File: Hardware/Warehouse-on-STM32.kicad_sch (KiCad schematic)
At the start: 22 parts, among them J1 ESP8266, J2 Conn_01x05, SW1 SW_Push, SW2 SW_Push, SW3 SW_Push, SW4 SW_Push, U1 STM32F103C8Tx, Y1 8MHz

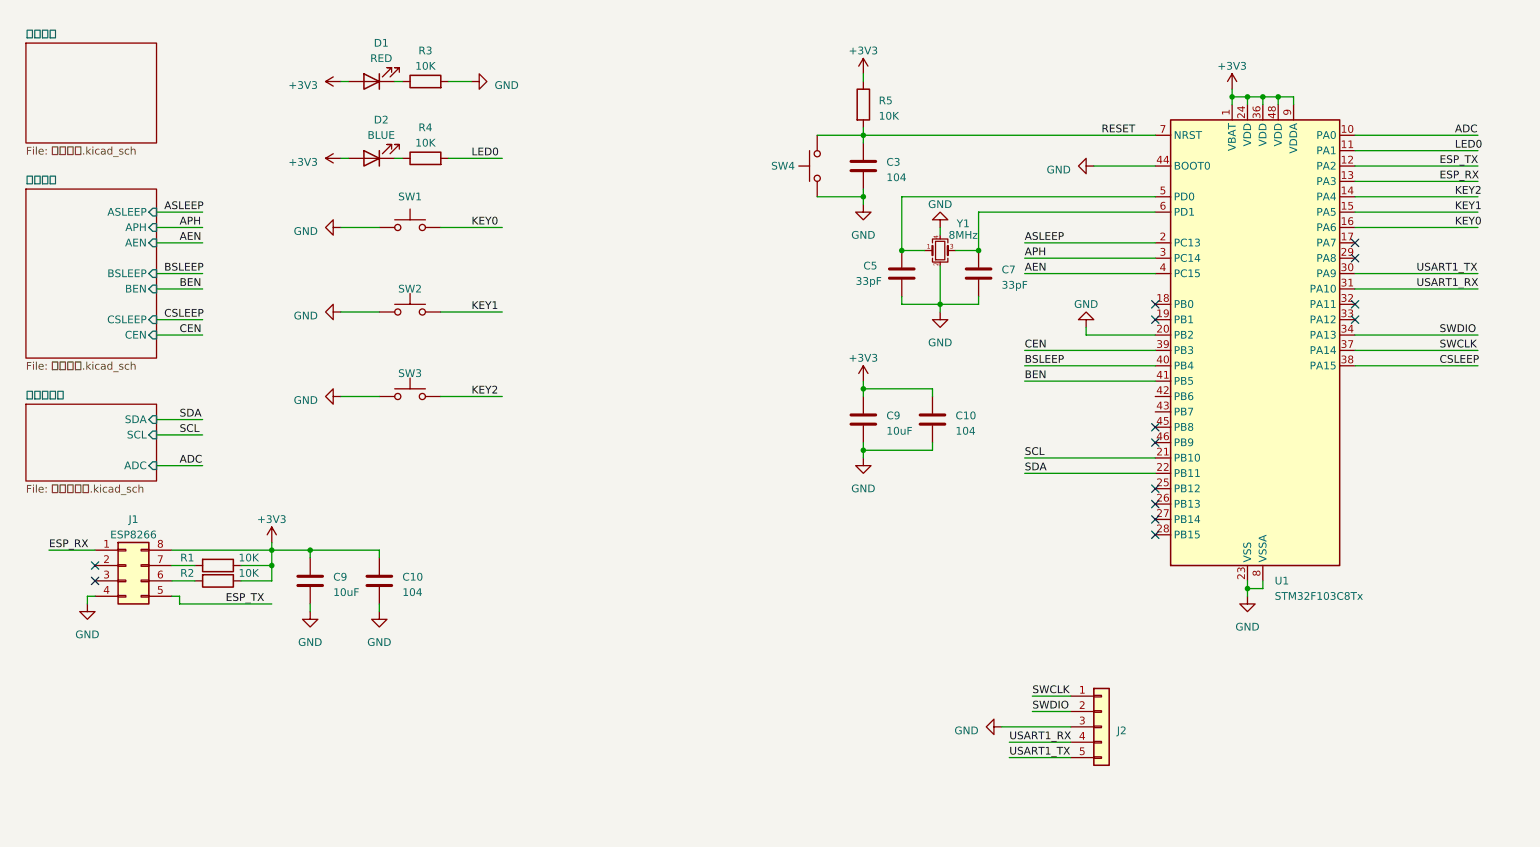
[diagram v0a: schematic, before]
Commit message: 修改了电机驱动芯片旁的电容封装为0603
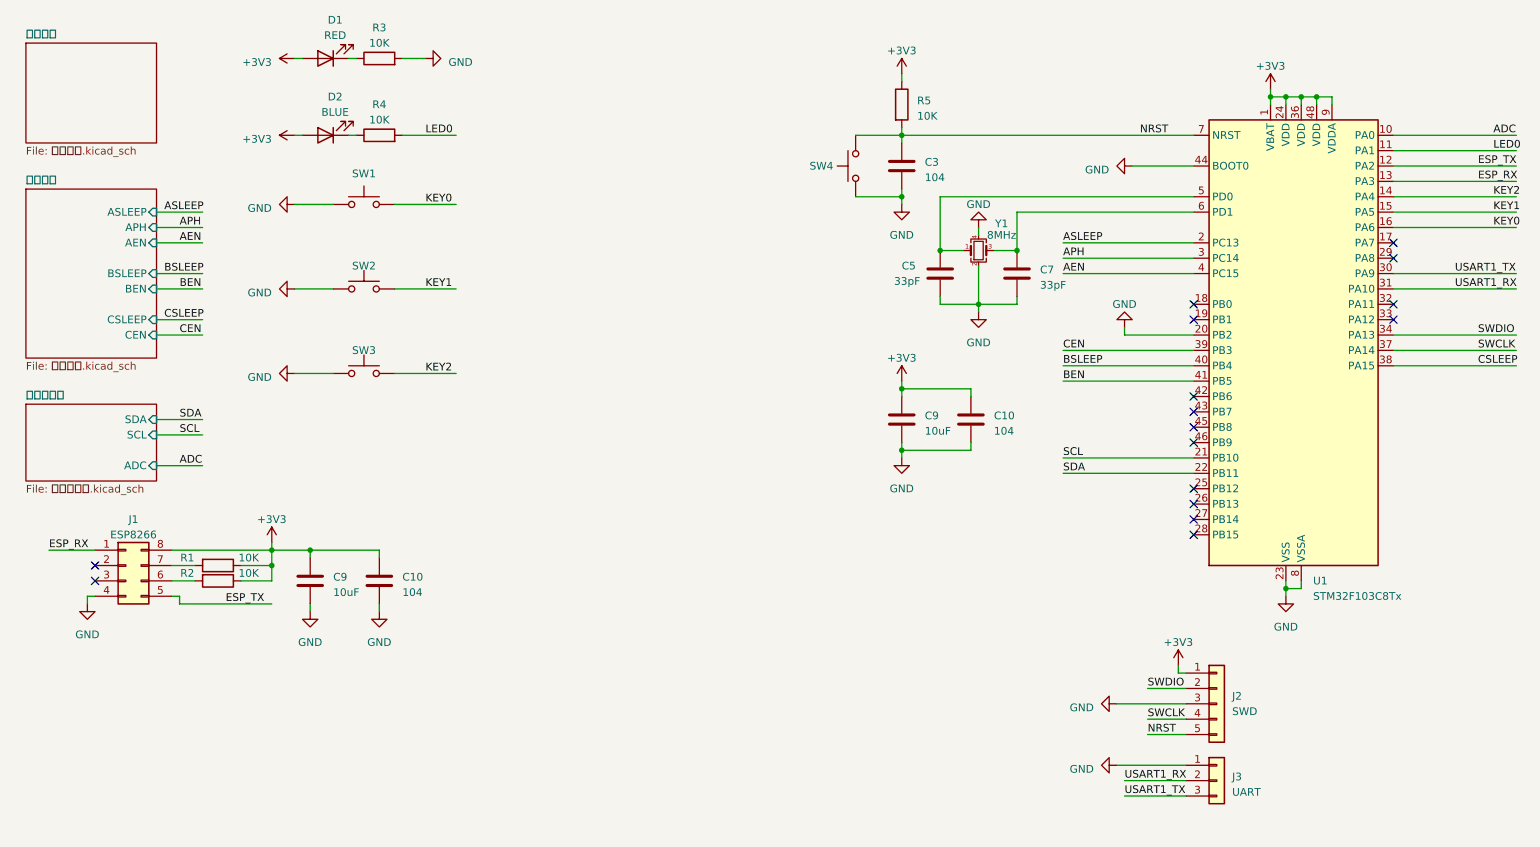
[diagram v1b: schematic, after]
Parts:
- added J3: UART, Connector_Molex:Molex_PicoBlade_53047-0210_1x02_P1.25mm_Vertical, symbol Connector_Generic:Conn_01x03
- J2: value Conn_01x05 -> SWD; footprint Connector_PinHeader_1.00mm:PinHeader_1x05_P1.00mm_Vertical -> Connector_Molex:Molex_PicoBlade_53047-0210_1x02_P1.25mm_Vertical
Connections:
- net +3V3: now also J2.1 (Pin_1)
- net GND: now also J3.1 (Pin_1)
- net SWCLK: now also J2.4 (Pin_4); no longer J2.1 (Pin_1)
- net USART1_RX: now also J3.2 (Pin_2); no longer J2.4 (Pin_4)
- net USART1_TX: now also J3.3 (Pin_3); no longer J2.5 (Pin_5)
- net RESET renamed NRST
- net NRST: now also J2.5 (Pin_5)
- no-connect marks 14 -> 16
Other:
- moved on the sheet: C10, C3, C5, C7, C9, D1, D2, R3, R4, R5, SW1, SW2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

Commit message: coding
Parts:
- J2: footprint Connector_Molex:Molex_PicoBlade_53047-0210_1x02_P1.25mm_Vertical -> Connector_Yource:1.25-5A
- J3: footprint Connector_Molex:Molex_PicoBlade_53047-0210_1x02_P1.25mm_Vertical -> Connector_Yource:1.25-3A
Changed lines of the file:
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@@
       (effects (font (size 1.27 1.27)) (justify left))
     )
-    (property "Footprint" "Connector_Molex:Molex_PicoBlade_53047-0210_1x02_P1.25mm_Vertical" (at 214.63 128.27 0)
+    (property "Footprint" "Connector_Yource:1.25-5A" (at 214.63 128.27 0)
       (effects (font (size 1.27 1.27)) hide)
     )
@@
       (effects (font (size 1.27 1.27)) (justify left))
     )
-    (property "Footprint" "Connector_Molex:Molex_PicoBlade_53047-0210_1x02_P1.25mm_Vertical" (at 214.63 140.97 0)
-      (effects (font (size 1.27 1.27)) hide)
-    )
+    (property "Footprint" "Connector_Yource:1.25-3A" (at 214.63 140.97 0)
+      (effects (font (size 1.27 1.27)) hide)
+    )

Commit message: update
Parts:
- added J8: Conn_01x05, symbol Connector_Generic:Conn_01x05
- added R6: 10K, Resistor_SMD:R_0402_1005Metric, symbol Device:R
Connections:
- net +3V3: now also J8.1 (Pin_1), R6.2
- net ESP_RX: now also J1.5 (Pin_5); no longer J1.1 (Pin_1)
- net ESP_TX: now also J1.1 (Pin_1); no longer J1.5 (Pin_5)
- net GND: now also J8.2 (Pin_2)
- net SCL: now also J8.3 (Pin_3)
- net SDA: now also J8.4 (Pin_4)
- new net: J8.5 (Pin_5), R6.1
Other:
- removed sheet 传感器模块
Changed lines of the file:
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@@
+    (stroke (width 0) (type default))
+  )
+  (wire (pts (xy 22.86 134.62) (xy 31.75 134.62))
+    (stroke (width 0) (type default))
+  )
+  (wire (pts (xy 25.4 132.08) (xy 31.75 132.08))
     (stroke (width 0) (type default))
   )
@@
     (stroke (width 0) (type default))
   )
+  (wire (pts (xy 22.86 124.46) (xy 22.86 123.19))
+    (stroke (width 0) (type default))
+  )
   (wire (pts (xy 162.56 76.2) (xy 173.99 76.2))
     (stroke (width 0) (type default))
@@
     (stroke (width 0) (type default))
   )
-  (wire (pts (xy 39.37 88.9) (xy 46.99 88.9))
-    (stroke (width 0) (type default))
-  )
   (wire (pts (xy 168.91 44.45) (xy 210.82 44.45))
     (stroke (width 0) (type default))
@@
     (stroke (width 0) (type default))
   )
+  (wire (pts (xy 31.75 124.46) (xy 22.86 124.46))
+    (stroke (width 0) (type default))
+  )
   (wire (pts (xy 53.34 107.95) (xy 58.42 107.95))
     (stroke (width 0) (type default))
@@
     (stroke (width 0) (type default))
   )
-  (wire (pts (xy 39.37 81.28) (xy 46.99 81.28))
-    (stroke (width 0) (type default))
-  )
   (wire (pts (xy 21.59 102.87) (xy 29.21 102.87))
     (stroke (width 0) (type default))
   )
+  (wire (pts (xy 22.86 142.24) (xy 22.86 143.51))
+    (stroke (width 0) (type default))
+  )
   (wire (pts (xy 243.84 57.15) (xy 264.16 57.15))
     (stroke (width 0) (type default))
@@
     (stroke (width 0) (type default))
   )
+  (wire (pts (xy 24.13 127) (xy 31.75 127))
+    (stroke (width 0) (type default))
+  )
   (wire (pts (xy 208.28 121.92) (xy 208.28 123.19))
     (stroke (width 0) (type default))
@@
     (stroke (width 0) (type default))
   )
-  (wire (pts (xy 39.37 83.82) (xy 46.99 83.82))
-    (stroke (width 0) (type default))
-  )
   (wire (pts (xy 162.56 85.09) (xy 162.56 86.36))
     (stroke (width 0) (type default))
@@
     (stroke (width 0) (type default))
   )
+  (wire (pts (xy 25.4 129.54) (xy 31.75 129.54))
+    (stroke (width 0) (type default))
+  )
   (wire (pts (xy 199.39 67.31) (xy 199.39 66.04))
     (stroke (width 0) (type default))
@@
     (effects (font (size 1.27 1.27)) (justify left bottom))
   )
+  (label "SDA" (at 25.4 132.08 0) (fields_autoplaced)
+    (effects (font (size 1.27 1.27)) (justify left bottom))
+  )
   (label "USART1_TX" (at 254 57.15 0) (fields_autoplaced)
     (effects (font (size 1.27 1.27)) (justify left bottom))
   )
-  (label "SCL" (at 43.18 83.82 0) (fields_autoplaced)
+  (label "ESP_RX" (at 49.53 111.76 0) (fields_autoplaced)
+    (effects (font (size 1.27 1.27)) (justify left bottom))
+  )
+  (label "ESP_TX" (at 21.59 102.87 0) (fields_autoplaced)
     (effects (font (size 1.27 1.27)) (justify left bottom))
   )
@@
     (effects (font (size 1.27 1.27)) (justify left bottom))
   )
-  (label "ESP_RX" (at 21.59 102.87 0) (fields_autoplaced)
-    (effects (font (size 1.27 1.27)) (justify left bottom))
-  )
   (label "KEY2" (at 260.35 44.45 0) (fields_autoplaced)
     (effects (font (size 1.27 1.27)) (justify left bottom))
@@
     (effects (font (size 1.27 1.27)) (justify left bottom))
   )
-  (label "SDA" (at 43.18 81.28 0) (fields_autoplaced)
+  (label "SCL" (at 25.4 129.54 0) (fields_autoplaced)
     (effects (font (size 1.27 1.27)) (justify left bottom))
   )
@@
   )
   (label "KEY1" (at 83.82 59.69 0) (fields_autoplaced)
-    (effects (font (size 1.27 1.27)) (justify left bottom))
-  )
-  (label "ADC" (at 43.18 88.9 0) (fields_autoplaced)
-    (effects (font (size 1.27 1.27)) (justify left bottom))
-  )
-  (label "ESP_TX" (at 50.8 111.76 0) (fields_autoplaced)
     (effects (font (size 1.27 1.27)) (justify left bottom))
   )
@@
     )
   )
+  (symbol (lib_id "power:+3V3") (at 22.86 123.19 0) (unit 1)
+    (in_bom yes) (on_board yes) (dnp no) (fields_autoplaced)
+    (property "Reference" "#PWR024" (at 22.86 127 0)
+      (effects (font (size 1.27 1.27)) hide)
+    )
+    (property "Value" "+3V3" (at 22.86 119.38 0)
+      (effects (font (size 1.27 1.27)))
+    )
+    (property "Footprint" "" (at 22.86 123.19 0)
+      (effects (font (size 1.27 1.27)) hide)
+    )
+    (property "Datasheet" "" (at 22.86 123.19 0)
+      (effects (font (size 1.27 1.27)) hide)
+    )
+    (pin "1")
+    (instances
+      (project "Warehouse-on-STM32"
+        (path "/2599b9a9-6312-402b-9c24-1e87744a4c70"
+          (reference "#PWR024") (unit 1)
+        )
+      )
+    )
+  )
   (symbol (lib_id "Device:C") (at 162.56 39.37 0) (unit 1)
     (in_bom yes) (on_board yes) (dnp no) (fields_autoplaced)
@@
         (path "/2599b9a9-6312-402b-9c24-1e87744a4c70"
           (reference "D1") (unit 1)
+        )
+      )
+    )
+  )
+  (symbol (lib_id "Device:R") (at 22.86 138.43 0) (unit 1)
+    (in_bom yes) (on_board yes) (dnp no)
+    (property "Reference" "R6" (at 19.05 138.43 0)
+      (effects (font (size 1.27 1.27)))
+    )
+    (property "Value" "10K" (at 26.67 138.43 0)
+      (effects (font (size 1.27 1.27)))
+    )
+    (property "Footprint" "Resistor_SMD:R_0402_1005Metric" (at 21.082 138.43 90)
+      (effects (font (size 1.27 1.27)) hide)
+    )
+    (property "Datasheet" "~" (at 22.86 138.43 0)
+      (effects (font (size 1.27 1.27)) hide)
+    )
+    (pin "1")
+    (pin "2")
+    (instances
+      (project "Warehouse-on-STM32"
+        (path "/2599b9a9-6312-402b-9c24-1e87744a4c70"
+          (reference "R6") (unit 1)
         )
       )
@@
     )
   )
+  (symbol (lib_id "power:GND") (at 24.13 127 270) (unit 1)
+    (in_bom yes) (on_board yes) (dnp no) (fields_autoplaced)
+    (property "Reference" "#PWR025" (at 17.78 127 0)
+      (effects (font (size 1.27 1.27)) hide)
+    )
+    (property "Value" "GND" (at 20.32 127.635 90)
+      (effects (font (size 1.27 1.27)) (justify right))
+    )
+    (property "Footprint" "" (at 24.13 127 0)
+      (effects (font (size 1.27 1.27)) hide)
+    )
+    (property "Datasheet" "" (at 24.13 127 0)
+      (effects (font (size 1.27 1.27)) hide)
+    )
+    (pin "1")
+    (instances
+      (project "Warehouse-on-STM32"
+        (path "/2599b9a9-6312-402b-9c24-1e87744a4c70"
+          (reference "#PWR025") (unit 1)
+        )
+      )
+    )
+  )
   (symbol (lib_id "Switch:SW_Push") (at 73.66 73.66 0) (unit 1)
     (in_bom yes) (on_board yes) (dnp no) (fields_autoplaced)
@@
         (path "/2599b9a9-6312-402b-9c24-1e87744a4c70"
           (reference "#PWR02") (unit 1)
+        )
+      )
+    )
+  )
+  (symbol (lib_id "power:+3V3") (at 22.86 143.51 180) (unit 1)
+    (in_bom yes) (on_board yes) (dnp no) (fields_autoplaced)
+    (property "Reference" "#PWR026" (at 22.86 139.7 0)
+      (effects (font (size 1.27 1.27)) hide)
+    )
+    (property "Value" "+3V3" (at 22.86 148.59 0)
+      (effects (font (size 1.27 1.27)))
+    )
+    (property "Footprint" "" (at 22.86 143.51 0)
+      (effects (font (size 1.27 1.27)) hide)
+    )
+    (property "Datasheet" "" (at 22.86 143.51 0)
+      (effects (font (size 1.27 1.27)) hide)
+    )
+    (pin "1")
+    (instances
+      (project "Warehouse-on-STM32"
+        (path "/2599b9a9-6312-402b-9c24-1e87744a4c70"
+          (reference "#PWR026") (unit 1)
         )
       )
@@
     )
   )
+  (symbol (lib_id "Connector_Generic:Conn_01x05") (at 36.83 129.54 0) (unit 1)
+    (in_bom yes) (on_board yes) (dnp no) (fields_autoplaced)
+    (property "Reference" "J8" (at 39.37 128.905 0)
+      (effects (font (size 1.27 1.27)) (justify left))
+    )
+    (property "Value" "Conn_01x05" (at 39.37 131.445 0)
+      (effects (font (size 1.27 1.27)) (justify left))
+    )
+    (property "Footprint" "" (at 36.83 129.54 0)
+      (effects (font (size 1.27 1.27)) hide)
+    )
+    (property "Datasheet" "~" (at 36.83 129.54 0)
+      (effects (font (size 1.27 1.27)) hide)
+    )
+    (pin "1")
+    (pin "2")
+    (pin "3")
+    (pin "4")
+    (pin "5")
+    (instances
+      (project "Warehouse-on-STM32"
+        (path "/2599b9a9-6312-402b-9c24-1e87744a4c70"
+          (reference "J8") (unit 1)
+        )
+      )
+    )
+  )
   (symbol (lib_id "power:GND") (at 76.2 113.03 0) (unit 1)
     (in_bom yes) (on_board yes) (dnp no) (fields_autoplaced)
@@
       )
     )
-  )
-  (sheet (at 17.78 78.74) (size 21.59 12.7) (fields_autoplaced)
-    (stroke (width 0.1524) (type solid))
-    (fill (color 0 0 0 0.0000))
-    (property "Sheetname" "传感器模块" (at 17.78 78.0284 0)
-      (effects (font (size 1.27 1.27)) (justify left bottom))
-    )
-    (property "Sheetfile" "传感器模块.kicad_sch" (at 17.78 92.0246 0)
-      (effects (font (size 1.27 1.27)) (justify left top))
-    )
-    (pin "SDA" input (at 39.37 81.28 0)
-      (effects (font (size 1.27 1.27)) (justify right))
-    )
-    (pin "SCL" input (at 39.37 83.82 0)
-      (effects (font (size 1.27 1.27)) (justify right))
-    )
-    (pin "ADC" input (at 39.37 88.9 0)
-      (effects (font (size 1.27 1.27)) (justify right))
-    )
-    (instances
-      (project "Warehouse-on-STM32"
-        (path "/2599b9a9-6312-402b-9c24-1e87744a4c70" (page "5"))
-      )
-    )
